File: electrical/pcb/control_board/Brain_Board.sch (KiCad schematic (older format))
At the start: 42 parts, among them J22 S9175-ND_rpi_breakout, J23 S9175-ND_rpi_breakout, J24 6posheader, J25 SSW-104-01-F-T, J26 PEC10DAAN, J27 PPTC021LFBN-RC, J28 PPTC021LFBN-RC, J29 PPTC021LFBN-RC, M1 Mounting_Holes, Q1 2N3906, Q2 2N3906, Q3 2N3906, SW1 CT206124-ND, U6 DC7G3HWA

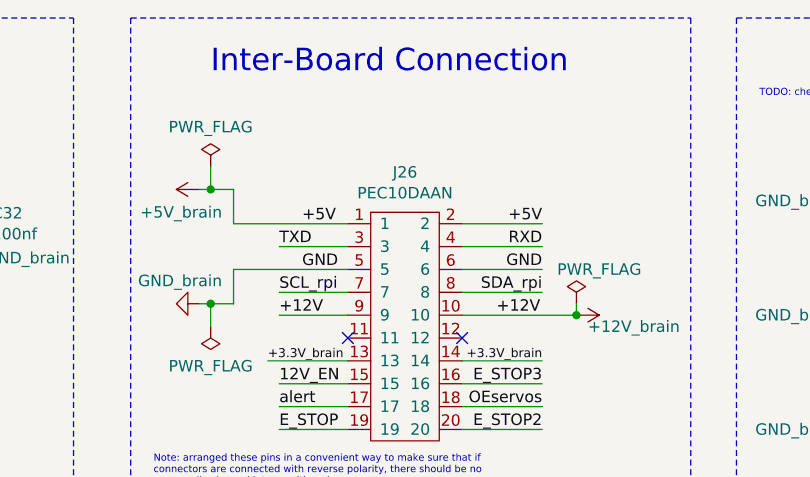
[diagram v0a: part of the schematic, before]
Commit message: Update PEC10DAAN to WM6548-ND
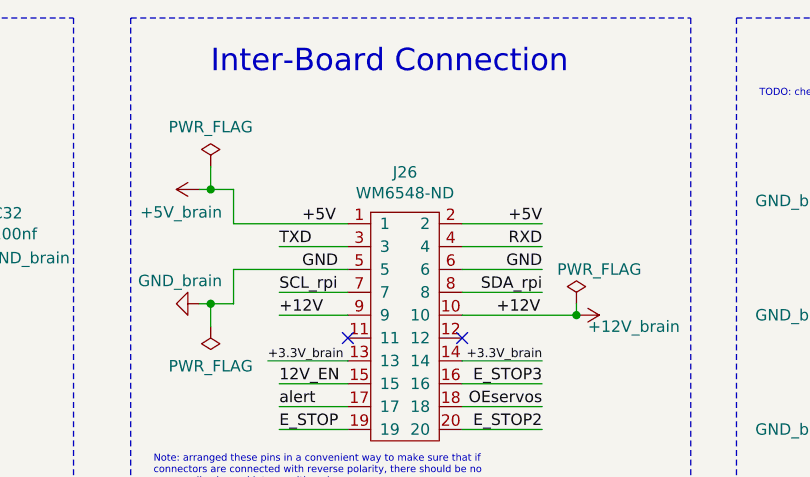
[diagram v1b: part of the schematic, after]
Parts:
- J26: value PEC10DAAN -> WM6548-ND
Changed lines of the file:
@@
 P 5650 1850
 F 0 "J26" H 5650 1925 50  0000 C CNN
-F 1 "PEC10DAAN" H 5650 1834 50  0000 C CNN
+F 1 "WM6548-ND" H 5650 1834 50  0000 C CNN
 F 2 "JPL Robotics:WM6548-ND" H 5950 1850 50  0001 C CNN
 F 3 "" H 5950 1850 50  0001 C CNN

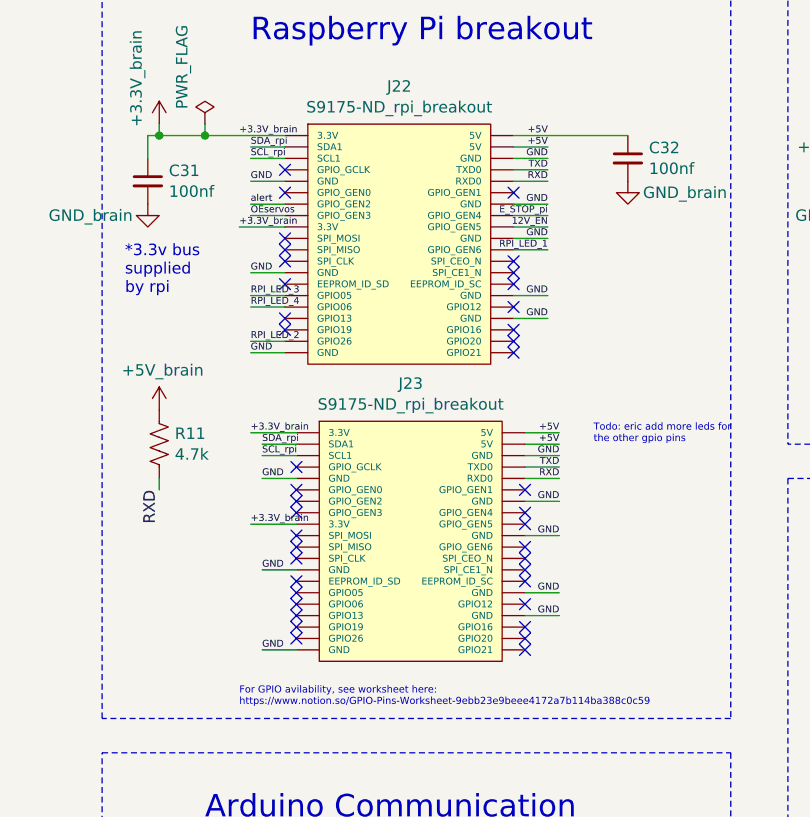
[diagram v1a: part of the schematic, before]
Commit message: Connecting all unused pins between rpi connector and rpi signal breakout
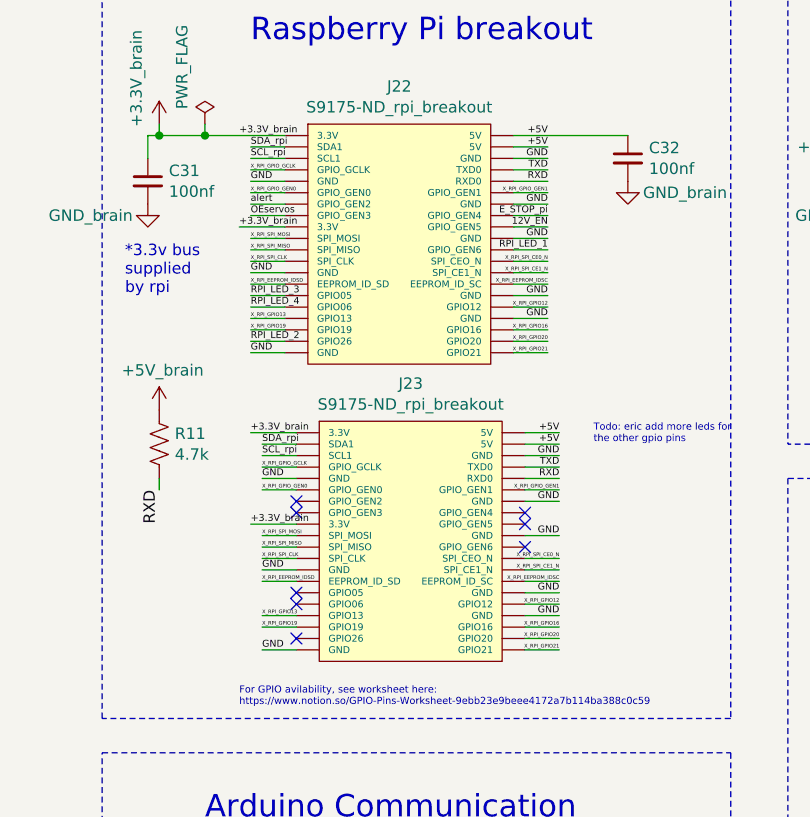
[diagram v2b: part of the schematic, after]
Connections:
- net X_RPI_GPIO_GEN0: now reaches J23.11 (GPIO_GEN0)
- net X_RPI_GPIO_GEN0: now also J22.11 (GPIO_GEN0)
- net X_RPI_GPIO_GEN1: now reaches J23.12 (GPIO_GEN1)
- net X_RPI_GPIO_GEN1: now also J22.12 (GPIO_GEN1)
- net X_RPI_SPI_MOSI: now reaches J23.19 (SPI_MOSI)
- net X_RPI_SPI_MOSI: now also J22.19 (SPI_MOSI)
- net X_RPI_SPI_MISO: now reaches J23.21 (SPI_MISO)
- net X_RPI_SPI_MISO: now also J22.21 (SPI_MISO)
- net X_RPI_SPI_CLK: now reaches J23.23 (SPI_CLK)
- net X_RPI_SPI_CLK: now also J22.23 (SPI_CLK)
- net X_RPI_SPI_CE0_N: now reaches J23.24 (SPI_CEO_N)
- net X_RPI_SPI_CE0_N: now also J22.24 (SPI_CEO_N)
- net X_RPI_SPI_CE1_N: now reaches J23.26 (SPI_CE1_N)
- net X_RPI_SPI_CE1_N: now also J22.26 (SPI_CE1_N)
- net X_RPI_EEPROM_IDSD: now reaches J23.27 (EEPROM_ID_SD)
- net X_RPI_EEPROM_IDSD: now also J22.27 (EEPROM_ID_SD)
- net X_RPI_EEPROM_IDSC: now reaches J23.28 (EEPROM_ID_SC)
- net X_RPI_EEPROM_IDSC: now also J22.28 (EEPROM_ID_SC)
- net X_RPI_GPIO12: now reaches J23.32 (GPIO12)
- net X_RPI_GPIO12: now also J22.32 (GPIO12)
- net X_RPI_GPIO13: now reaches J23.33 (GPIO13)
- net X_RPI_GPIO13: now also J22.33 (GPIO13)
- net X_RPI_GPIO19: now reaches J23.35 (GPIO19)
- net X_RPI_GPIO19: now also J22.35 (GPIO19)
- net X_RPI_GPIO16: now reaches J23.36 (GPIO16)
- net X_RPI_GPIO16: now also J22.36 (GPIO16)
- net X_RPI_GPIO20: now reaches J23.38 (GPIO20)
- net X_RPI_GPIO20: now also J22.38 (GPIO20)
- net X_RPI_GPIO21: now reaches J23.40 (GPIO21)
- net X_RPI_GPIO21: now also J22.40 (GPIO21)
- net X_RPI_GPIO_GCLK: now reaches J23.7 (GPIO_GCLK)
- net X_RPI_GPIO_GCLK: now also J22.7 (GPIO_GCLK)
- no-connect marks 47 -> 15
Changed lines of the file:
@@
 	2800 5400 3050 5400
 NoConn ~ 2800 5500
-NoConn ~ 2250 2350
-NoConn ~ 2250 2450
-NoConn ~ 2250 2400
-NoConn ~ 3250 2450
-NoConn ~ 3250 2500
-NoConn ~ 2300 3650
-NoConn ~ 2300 3700
-NoConn ~ 2300 3750
-NoConn ~ 3300 3750
-NoConn ~ 3300 3800
 $Comp
 L power:PWR_FLAG #FLG06
@@
 Text Notes 1550 2600 0    50   ~ 0
 *3.3v bus \nsupplied\nby rpi
-NoConn ~ 2250 2050
-NoConn ~ 2250 2550
-NoConn ~ 2250 2700
-NoConn ~ 2250 2750
-NoConn ~ 3250 2650
-NoConn ~ 3250 2800
-NoConn ~ 3250 2750
-NoConn ~ 3250 2850
-NoConn ~ 3250 2550
-NoConn ~ 3250 2150
-NoConn ~ 2300 3350
-NoConn ~ 2300 3850
 NoConn ~ 2300 3900
 NoConn ~ 2300 3950
-NoConn ~ 2300 4000
-NoConn ~ 2300 4050
 NoConn ~ 2300 4100
-NoConn ~ 3300 4150
-NoConn ~ 3300 4100
-NoConn ~ 3300 4050
-NoConn ~ 3300 3950
-NoConn ~ 3300 3850
 NoConn ~ 3300 3700
 NoConn ~ 3300 3600
-NoConn ~ 3300 3450
 Text Notes 4800 1350 0    98   ~ 0
 Inter-Board Connection
@@
 Wire Notes Line
 	6900 5200 6900 3400
-NoConn ~ 2300 3450
-NoConn ~ 2250 2150
 Wire Wire Line
 	2250 2250 2100 2250
@@
 Wire Notes Line
 	10350 5300 10350 6400
-$Comp
-L JPL_Robotics_Lib:S9175-ND_rpi_breakout J22
-U 1 1 60A8A979
-P 2150 3000
-F 0 "J22" H 2750 4315 50  0000 C CNN
-F 1 "S9175-ND_rpi_breakout" H 2750 4224 50  0000 C CNN
-F 2 "JPL Robotics:S9175-ND" H 2400 4250 50  0001 C CNN
-F 3 "" H 2400 4250 50  0001 C CNN
-	1    2150 3000
-	1    0    0    -1
-$EndComp
 Text Label 3400 2400 2    30   ~ 0
 RPI_LED_1
@@
 Wire Wire Line
 	5150 6500 5300 6500
+Wire Wire Line
+	2250 2050 2100 2050
+Text Label 2100 2050 0    16   ~ 0
+X_RPI_GPIO_GCLK
+Wire Wire Line
+	2300 3350 2150 3350
+Text Label 2150 3350 0    16   ~ 0
+X_RPI_GPIO_GCLK
+$Comp
+L JPL_Robotics_Lib:S9175-ND_rpi_breakout J22
+U 1 1 60A8A979
+P 2150 3000
+F 0 "J22" H 2750 4315 50  0000 C CNN
+F 1 "S9175-ND_rpi_breakout" H 2750 4224 50  0000 C CNN
+F 2 "JPL Robotics:S9175-ND" H 2400 4250 50  0001 C CNN
+F 3 "" H 2400 4250 50  0001 C CNN
+	1    2150 3000
+	1    0    0    -1
+$EndComp
+Text Label 2100 2150 0    16   ~ 0
+X_RPI_GPIO_GEN0
+Wire Wire Line
+	2250 2150 2100 2150
+Text Label 2100 2350 0    16   ~ 0
+X_RPI_SPI_MOSI
+Text Label 2100 2400 0    16   ~ 0
+X_RPI_SPI_MISO
+Text Label 2100 2550 0    16   ~ 0
+X_RPI_EEPROM_IDSD
+Text Label 2100 2700 0    16   ~ 0
+X_RPI_GPIO13
+Text Label 2100 2750 0    16   ~ 0
+X_RPI_GPIO19
+Text Label 3400 2150 2    16   ~ 0
+X_RPI_GPIO_GEN1
+Text Label 3400 2650 2    16   ~ 0
+X_RPI_GPIO12
+Text Label 3400 2750 2    16   ~ 0
+X_RPI_GPIO16
+Text Label 3400 2800 2    16   ~ 0
+X_RPI_GPIO20
+Text Label 3400 2850 2    16   ~ 0
+X_RPI_GPIO21
+Text Label 2100 2450 0    16   ~ 0
+X_RPI_SPI_CLK
+Text Label 3400 2550 2    16   ~ 0
+X_RPI_EEPROM_IDSC
+Text Label 3400 2450 2    16   ~ 0
+X_RPI_SPI_CE0_N
+Text Label 3400 2500 2    16   ~ 0
+X_RPI_SPI_CE1_N
+Wire Wire Line
+	2250 2350 2100 2350
+Wire Wire Line
+	2250 2400 2100 2400
+Wire Wire Line
+	2100 2450 2250 2450
+Wire Wire Line
+	2100 2550 2250 2550
+Wire Wire Line
+	2100 2700 2250 2700
+Wire Wire Line
+	2100 2750 2250 2750
+Wire Wire Line
+	3250 2150 3400 2150
+Wire Wire Line
+	3250 2450 3400 2450
+Wire Wire Line
+	3250 2650 3400 2650
+Wire Wire Line
+	3250 2550 3400 2550
+Wire Wire Line
+	3250 2500 3400 2500
+Wire Wire Line
+	3250 2750 3400 2750
+Wire Wire Line
+	3250 2800 3400 2800
+Wire Wire Line
+	3250 2850 3400 2850
+Text Label 3450 4150 2    16   ~ 0
+X_RPI_GPIO21
+Text Label 3450 4100 2    16   ~ 0
+X_RPI_GPIO20
+Text Label 3450 4050 2    16   ~ 0
+X_RPI_GPIO16
+Text Label 3450 3950 2    16   ~ 0
+X_RPI_GPIO12
+Text Label 3450 3850 2    16   ~ 0
+X_RPI_EEPROM_IDSC
+Text Label 3450 3800 2    16   ~ 0
+X_RPI_SPI_CE1_N
+Text Label 3450 3750 2    16   ~ 0
+X_RPI_SPI_CE0_N
+Text Label 3450 3450 2    16   ~ 0
+X_RPI_GPIO_GEN1
+Text Label 2150 4050 0    16   ~ 0
+X_RPI_GPIO19
+Text Label 2150 4000 0    16   ~ 0
+X_RPI_GPIO13
+Text Label 2150 3850 0    16   ~ 0
+X_RPI_EEPROM_IDSD
+Text Label 2150 3750 0    16   ~ 0
+X_RPI_SPI_CLK
+Text Label 2150 3700 0    16   ~ 0
+X_RPI_SPI_MISO
+Text Label 2150 3650 0    16   ~ 0
+X_RPI_SPI_MOSI
+Text Label 2150 3450 0    16   ~ 0
+X_RPI_GPIO_GEN0
+Wire Wire Line
+	2150 3450 2300 3450
+Wire Wire Line
+	2150 3650 2300 3650
+Wire Wire Line
+	2150 3700 2300 3700
+Wire Wire Line
+	2150 3750 2300 3750
+Wire Wire Line
+	2150 3850 2300 3850
+Wire Wire Line
+	2150 4000 2300 4000
+Wire Wire Line
+	2150 4050 2300 4050
+Wire Wire Line
+	3300 3450 3450 3450
+Wire Wire Line
+	3300 3750 3450 3750
+Wire Wire Line
+	3300 3800 3450 3800
+Wire Wire Line
+	3300 3850 3450 3850
+Wire Wire Line
+	3300 3950 3450 3950
+Wire Wire Line
+	3300 4050 3450 4050
+Wire Wire Line
+	3300 4100 3450 4100
+Wire Wire Line
+	3300 4150 3450 4150
 $EndSCHEMATC

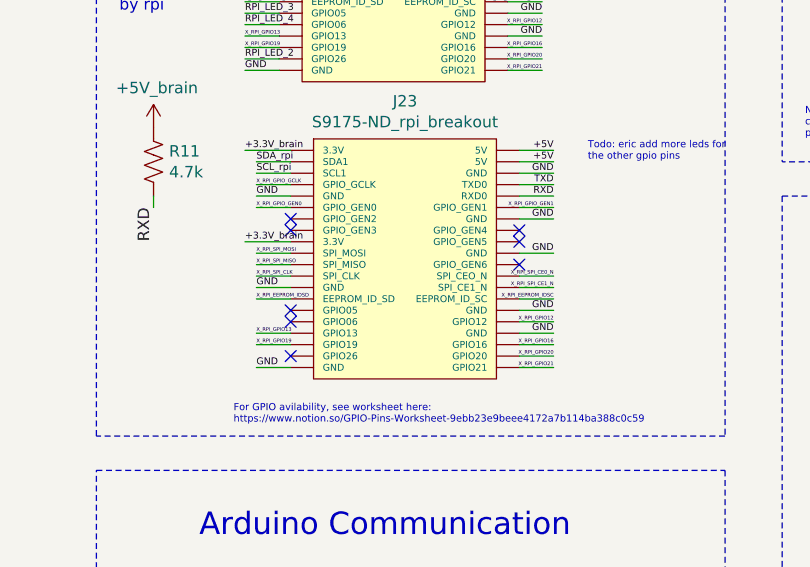
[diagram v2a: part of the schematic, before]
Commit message: Now connected all pins between rpi connector and singal breakout. Now they are equivalent, and both are rpi connectors.
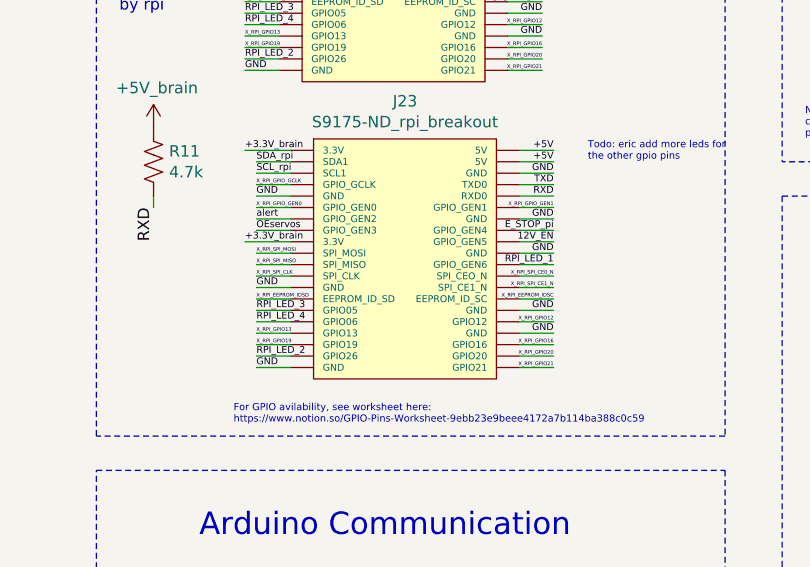
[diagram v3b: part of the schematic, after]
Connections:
- net 12V_EN: now also J23.18 (GPIO_GEN5)
- net E_STOP_pi: now also J23.16 (GPIO_GEN4)
- net OEservos: now also J23.15 (GPIO_GEN3)
- net RPI_LED_1: now also J23.22 (GPIO_GEN6)
- net RPI_LED_2: now also J23.37 (GPIO26)
- net RPI_LED_3: now also J23.29 (GPIO05)
- net RPI_LED_4: now also J23.31 (GPIO06)
- net alert: now also J23.13 (GPIO_GEN2)
- no-connect marks 15 -> 7
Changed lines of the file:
@@
 Text Label 3400 2250 2    30   ~ 0
 E_STOP_pi
-$Comp
-L JPL_Robotics_Lib:S9175-ND_rpi_breakout J23
-U 1 1 60A8A8FC
-P 2200 4300
-F 0 "J23" H 2800 5615 50  0000 C CNN
-F 1 "S9175-ND_rpi_breakout" H 2800 5524 50  0000 C CNN
-F 2 "JPL Robotics:S9175-ND" H 2450 5550 50  0001 C CNN
-F 3 "" H 2450 5550 50  0001 C CNN
-	1    2200 4300
-	1    0    0    -1
-$EndComp
 Wire Wire Line
 	2300 3400 2150 3400
@@
 Text Notes 1550 2600 0    50   ~ 0
 *3.3v bus \nsupplied\nby rpi
-NoConn ~ 2300 3900
-NoConn ~ 2300 3950
-NoConn ~ 2300 4100
-NoConn ~ 3300 3700
-NoConn ~ 3300 3600
 Text Notes 4800 1350 0    98   ~ 0
 Inter-Board Connection
@@
 Wire Wire Line
 	4900 1850 4900 2000
-NoConn ~ 3300 3550
 Wire Notes Line
 	4450 1100 4450 3250
@@
 Wire Wire Line
 	5900 2600 6250 2600
-NoConn ~ 2300 3500
-NoConn ~ 2300 3550
 Text Notes 2850 6100 0    98   ~ 0
 RPi I2C Header
@@
 Wire Wire Line
 	3300 4150 3450 4150
+$Comp
+L JPL_Robotics_Lib:S9175-ND_rpi_breakout J23
+U 1 1 60A8A8FC
+P 2200 4300
+F 0 "J23" H 2800 5615 50  0000 C CNN
+F 1 "S9175-ND_rpi_breakout" H 2800 5524 50  0000 C CNN
+F 2 "JPL Robotics:S9175-ND" H 2450 5550 50  0001 C CNN
+F 3 "" H 2450 5550 50  0001 C CNN
+	1    2200 4300
+	1    0    0    -1
+$EndComp
+Text Label 2150 3500 0    30   ~ 0
+alert
+Text Label 2150 3550 0    30   ~ 0
+OEservos
+Wire Wire Line
+	2150 3550 2300 3550
+Wire Wire Line
+	2150 3500 2300 3500
+Text Label 2150 3900 0    30   ~ 0
+RPI_LED_3
+Text Label 2150 3950 0    30   ~ 0
+RPI_LED_4
+Text Label 2150 4100 0    30   ~ 0
+RPI_LED_2
+Text Label 3450 3550 2    30   ~ 0
+E_STOP_pi
+Text Label 3450 3600 2    30   ~ 0
+12V_EN
+Text Label 3450 3700 2    30   ~ 0
+RPI_LED_1
+Wire Wire Line
+	2150 3900 2300 3900
+Wire Wire Line
+	2150 3950 2300 3950
+Wire Wire Line
+	2150 4100 2300 4100
+Wire Wire Line
+	3300 3550 3450 3550
+Wire Wire Line
+	3300 3600 3450 3600
+Wire Wire Line
+	3300 3700 3450 3700
 $EndSCHEMATC

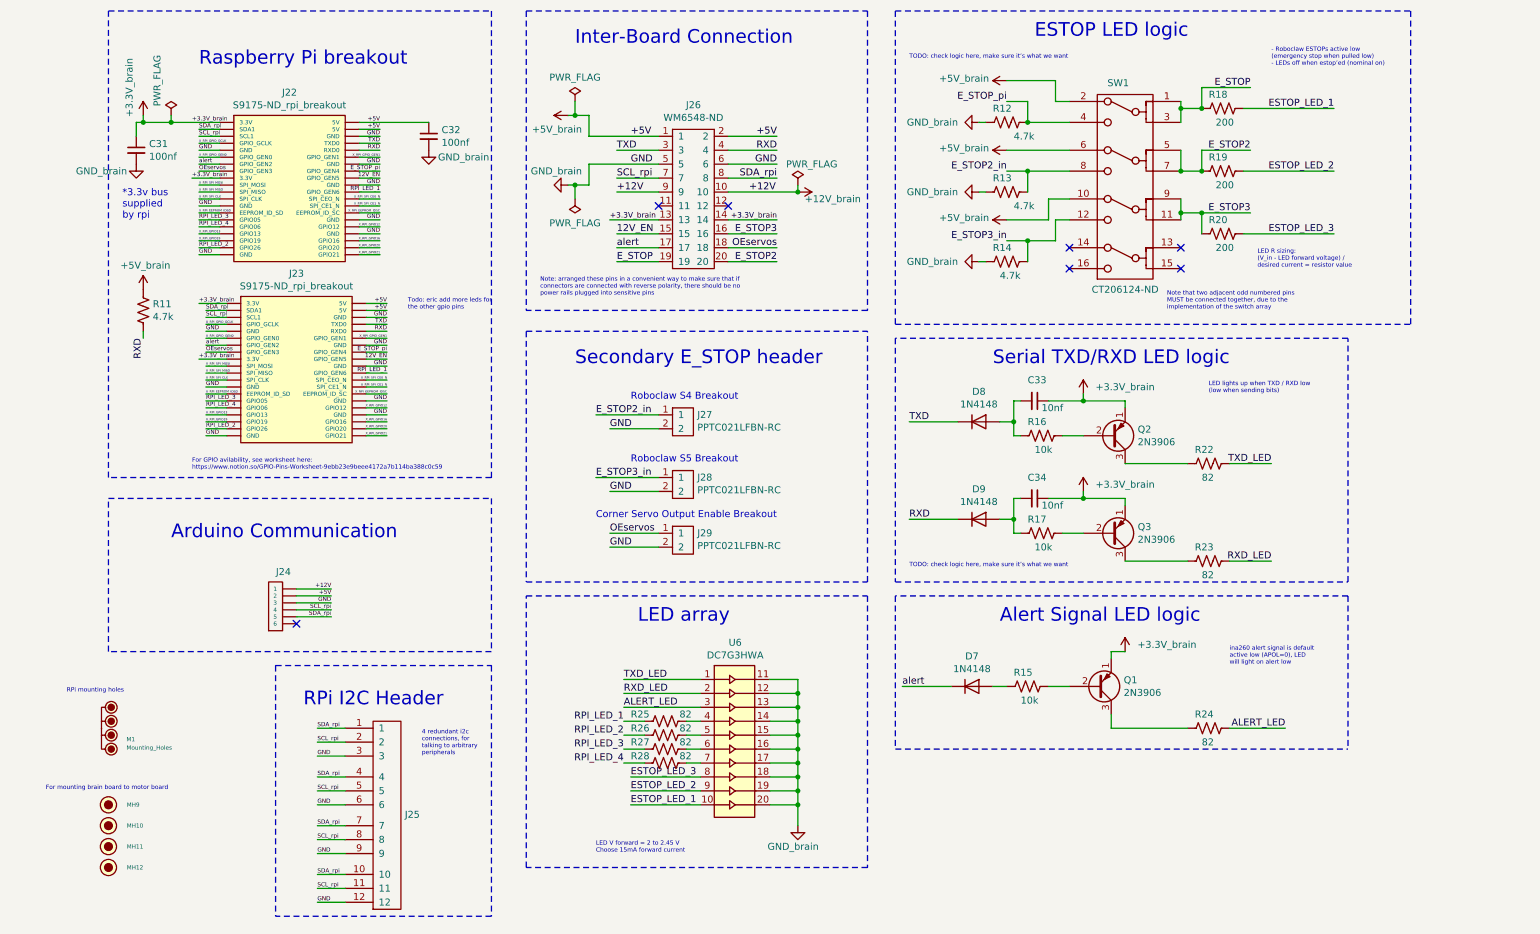
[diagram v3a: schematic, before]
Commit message: Refactor the test points, in particular added an array of test points for motor board. Add a couple of bigger test point footprints as well
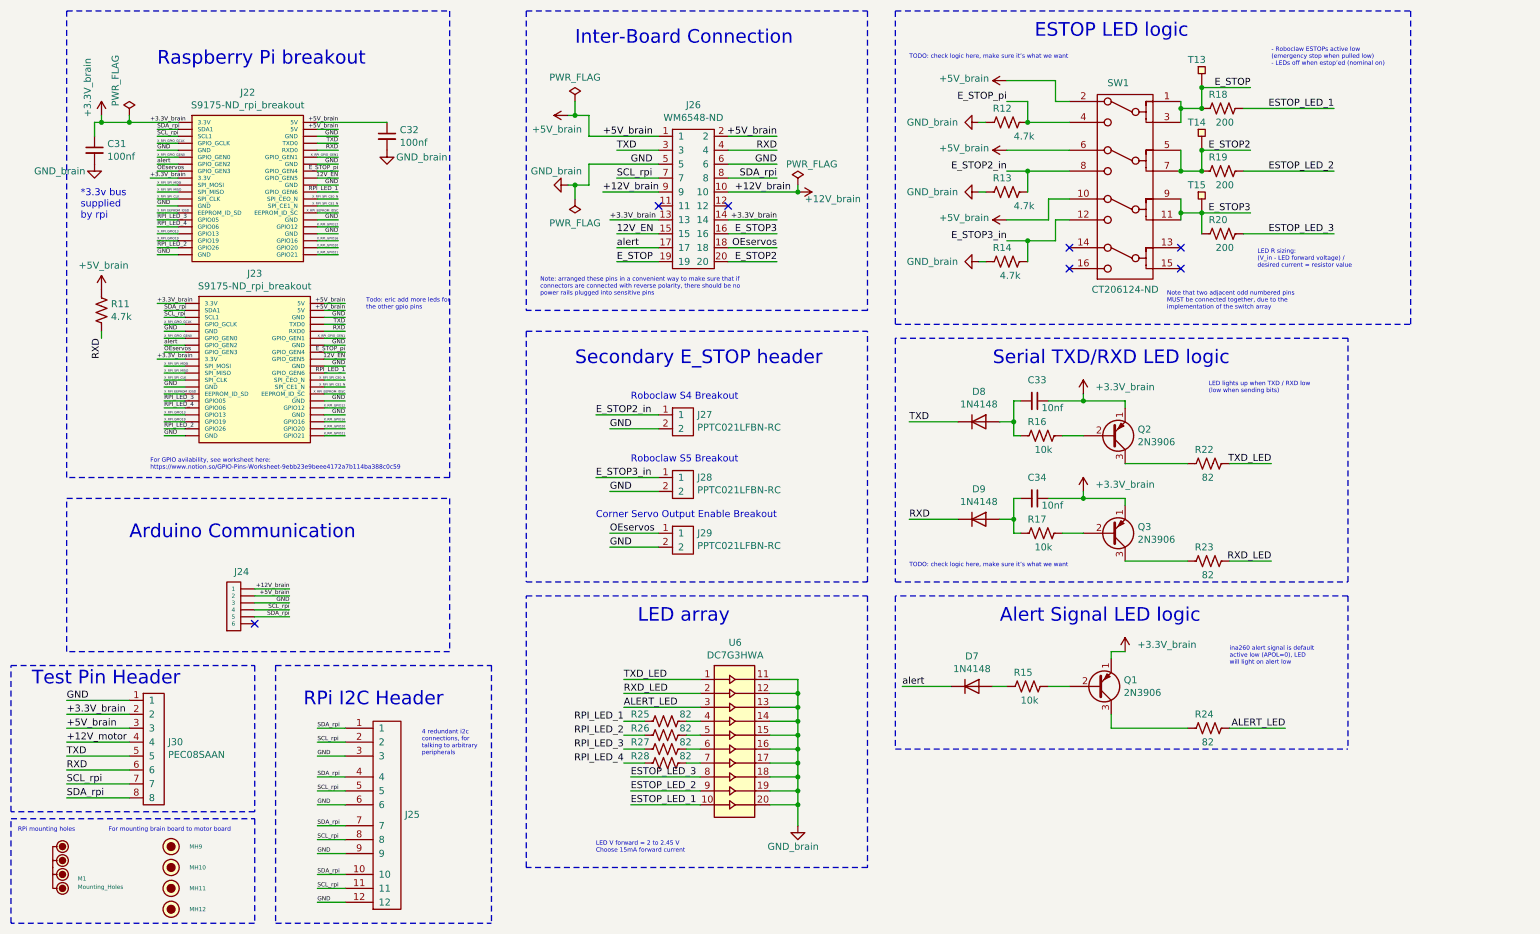
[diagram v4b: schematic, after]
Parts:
- added J30: PEC08SAAN, Connector_PinHeader_2.54mm:PinHeader_1x08_P2.54mm_Vertical, symbol JPL_Robotics_Lib:PEC08SAAN
- added T13, T14, T15: test_point, JPL Robotics:test_point, symbol JPL_Robotics_Lib:test_point
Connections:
- net +3.3V_brain: now also J30.2
- net +5V_brain: now also J30.3
- net E_STOP: now also T13.1
- net E_STOP2: now also T14.1
- net E_STOP3: now also T15.1
- net GND_brain: now also J30.1
- net RXD: now also J30.6
- net SCL_rpi: now also J30.7
- net SDA_rpi: now also J30.8
- net TXD: now also J30.5
- new net +12V_motor: J30.4
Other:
- note added: "Test Pin Header"
- moved on the sheet: C31, C32, J22, J23, J24, M1, MH10, MH11, MH12, MH9, R11
